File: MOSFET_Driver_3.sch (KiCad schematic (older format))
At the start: 20 parts, among them Q10 TPHR8504PL, Q11 TPHR8504PL, Q12 TPHR8504PL, Q7 TPHR8504PL, Q8 TPHR8504PL, Q9 TPHR8504PL, U1 FD6288Q

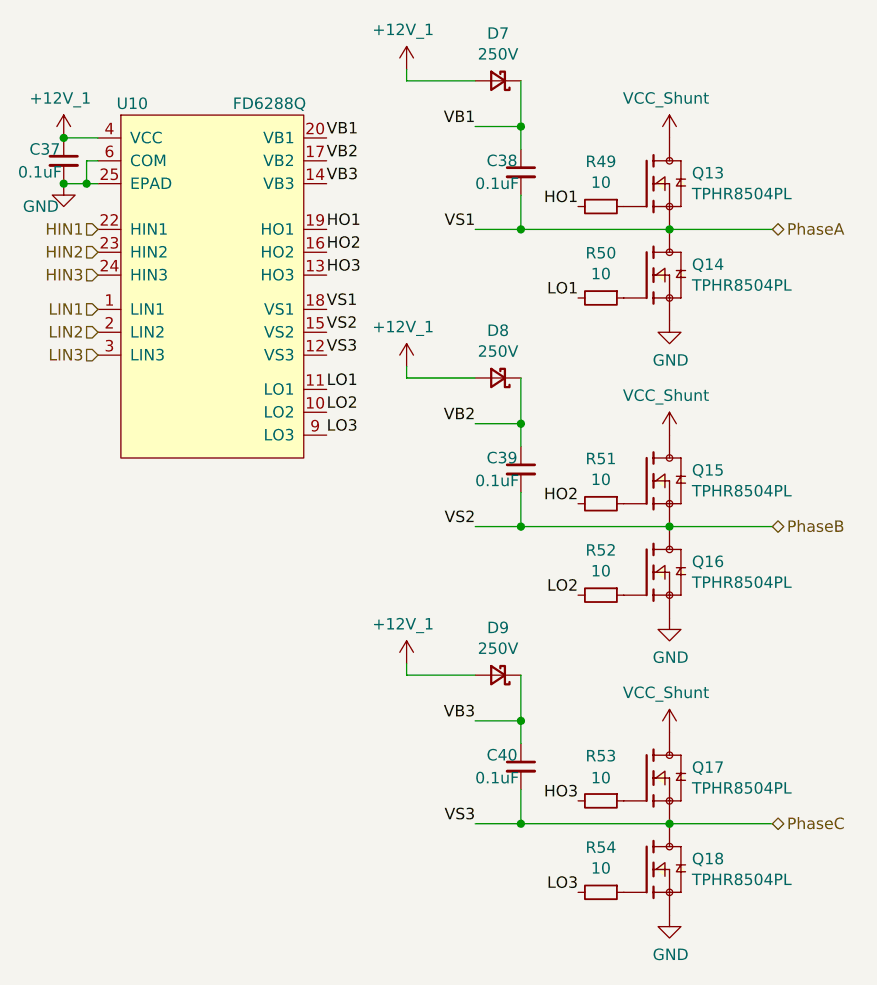
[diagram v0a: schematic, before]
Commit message: Lots of changes made with back being rerouted
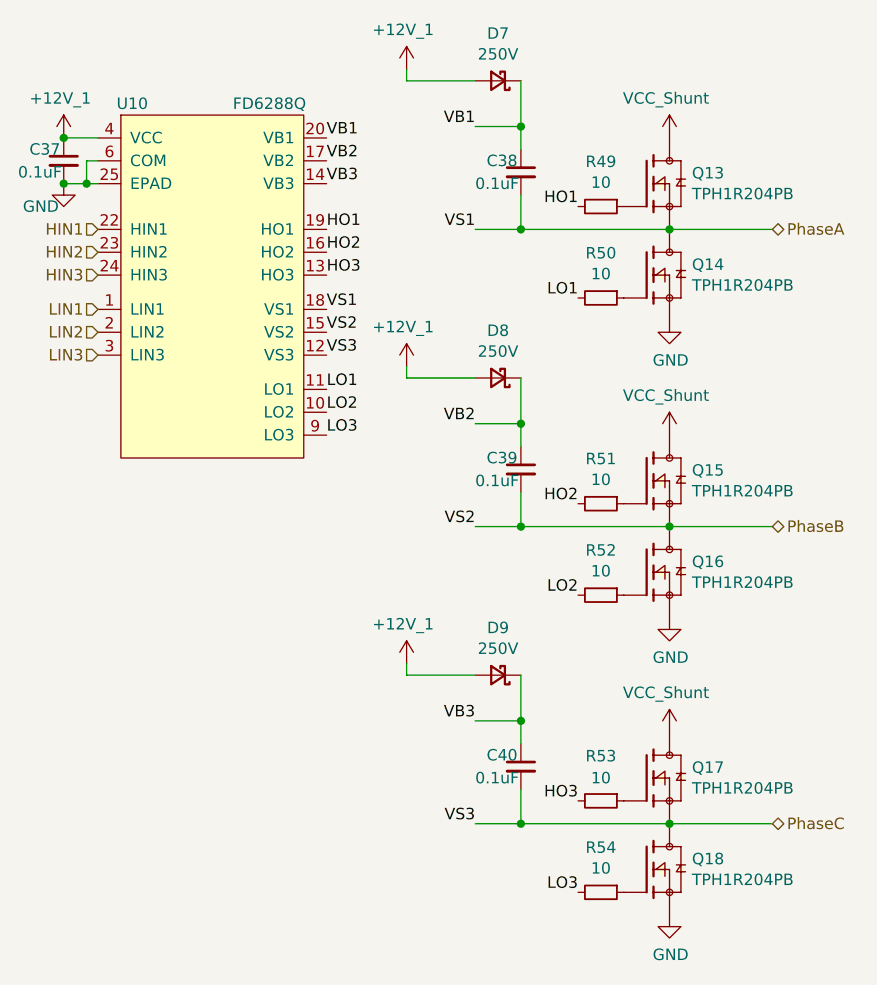
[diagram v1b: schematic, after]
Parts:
- removed Q10, Q11, Q12, Q7, Q8, Q9: TPHR8504PL, Footprints:TPHR8504PL, symbol JPW_Symbols:TPHR8504PL
- added Q13, Q14, Q15, Q16, Q17, Q18: TPH1R204PB, Footprints:TPH1R204PB, symbol JPW_Symbols:TPH1R204PB
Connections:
- net GND: now also Q14.1, Q14.2, Q14.3, Q16.1, Q16.2, Q16.3, Q18.1, Q18.2, Q18.3
- net PhaseA: now also Q13.1, Q13.2, Q13.3, Q14.5, Q14.6, Q14.7, Q14.8, Q14.9
- net PhaseB: now also Q15.1, Q15.2, Q15.3, Q16.5, Q16.6, Q16.7, Q16.8, Q16.9
- net PhaseC: now also Q17.1, Q17.2, Q17.3, Q18.5, Q18.6, Q18.7, Q18.8, Q18.9
- net VCC_Shunt: now also Q13.5, Q13.6, Q13.7, Q13.8, Q13.9, Q15.5, Q15.6, Q15.7, Q15.8, Q15.9, Q17.5, Q17.6, Q17.7, Q17.8, Q17.9
- net at R9.1: now also Q15.4
- net at R12.1: now also Q18.4
- net at R7.1: now also Q13.4
- net at R8.1: now also Q14.4
- net at R10.1: now also Q16.4
- net at R11.1: now also Q17.4
